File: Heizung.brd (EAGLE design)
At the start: 100 x 80 mm, 33 parts, among them IC1 MEGA8-PTQFP, Q2 2N7002, Q3 2N7002

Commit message: Floating wires are bad for you
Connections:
- removed net N$41: J_1.1, J_2.1, J_3.1, J_4.1
- net GND: now also J_1.1, J_2.1, J_3.1, J_4.1
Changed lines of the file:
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@@
 <via x="23.375" y="44.375" extent="1-16" drill="0.6" shape="square"/>
 <via x="40" y="47" extent="1-16" drill="0.6" shape="square"/>
+<contactref element="J_2" pad="1"/>
+<contactref element="J_1" pad="1"/>
+<contactref element="J_3" pad="1"/>
+<contactref element="J_4" pad="1"/>
 </signal>
 <signal name="N$141">
@@
 <wire x1="30.0823" y1="45.1461" x2="30.0823" y2="43.5055" width="0.35" layer="16"/>
 </signal>
-<signal name="N$41" class="1">
-<contactref element="J_2" pad="1"/>
-<contactref element="J_1" pad="1"/>
-<contactref element="J_3" pad="1"/>
-<contactref element="J_4" pad="1"/>
-<wire x1="40" y1="62.73" x2="40" y2="68.73" width="0" layer="19" extent="1-1"/>
-<wire x1="40" y1="56.73" x2="40" y2="62.73" width="0" layer="19" extent="1-1"/>
-<wire x1="40" y1="50.73" x2="40" y2="56.73" width="0" layer="19" extent="1-1"/>
-</signal>
 </signals>

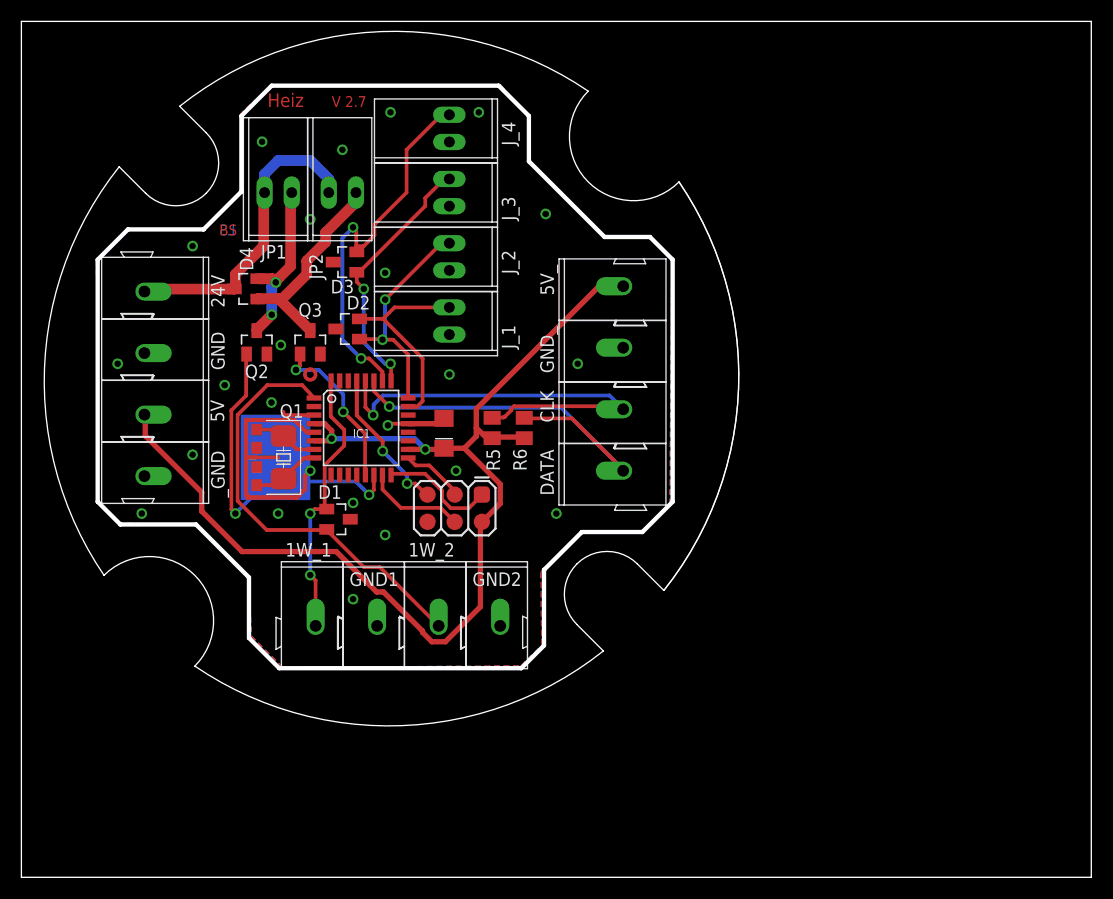
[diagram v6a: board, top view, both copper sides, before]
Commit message: 1x2 connectors wider, board outline more symmetric
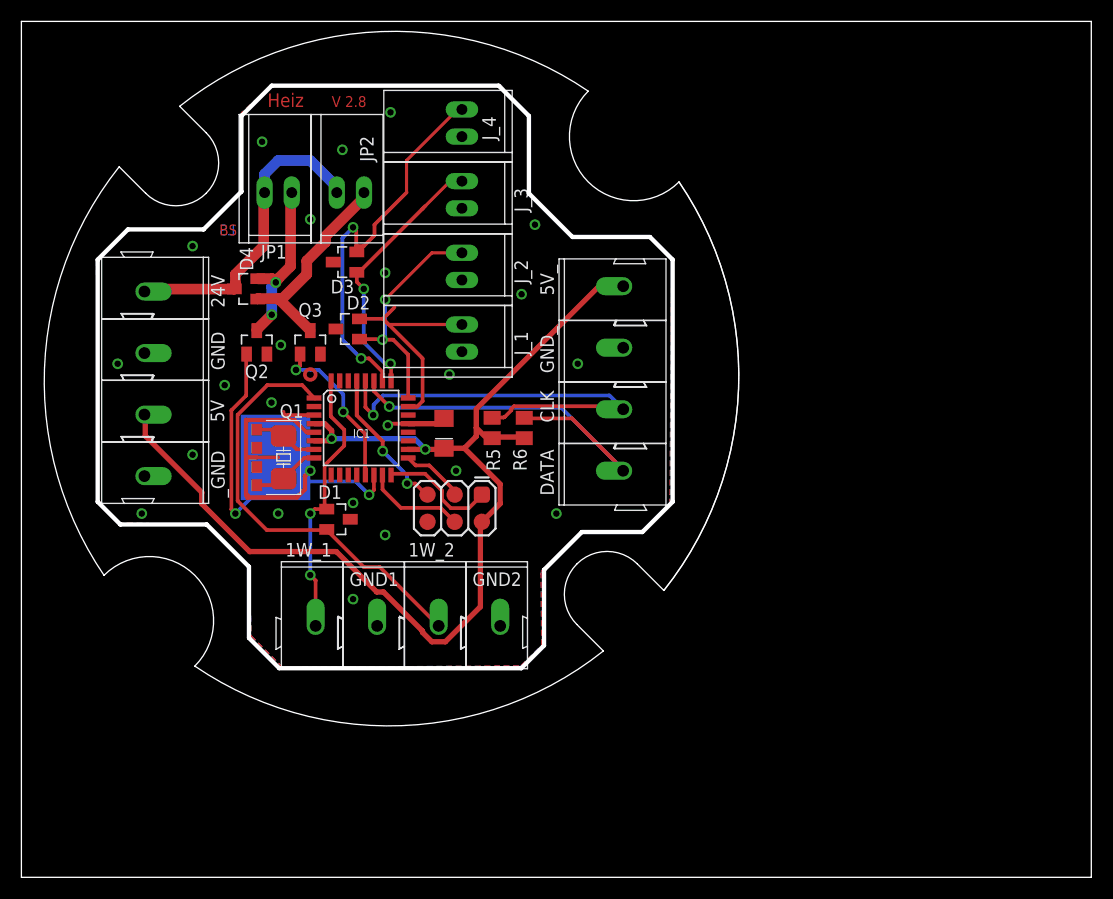
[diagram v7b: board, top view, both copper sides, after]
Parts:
- moved J_1 1.99 mm to (41.2, 50.4)
- moved J_2 1.48 mm to (41.2, 57.1)
- moved J_4 1.28 mm to (41.2, 70.5)
- moved J_3 1.19 mm to (41.2, 63.8)
- moved JP2 0.75 mm to (30.8, 64.0)
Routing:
- net B1: track 19.6 -> 21.8 mm
- net B3: track 24.5 -> 25.5 mm
- net B2: track 21.2 -> 22.0 mm
- net B4: track 35.9 -> 36.7 mm
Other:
- outline, holes or cut-outs redrawn
- board text added: "V 2.8"
- board text removed: "V 2.7"

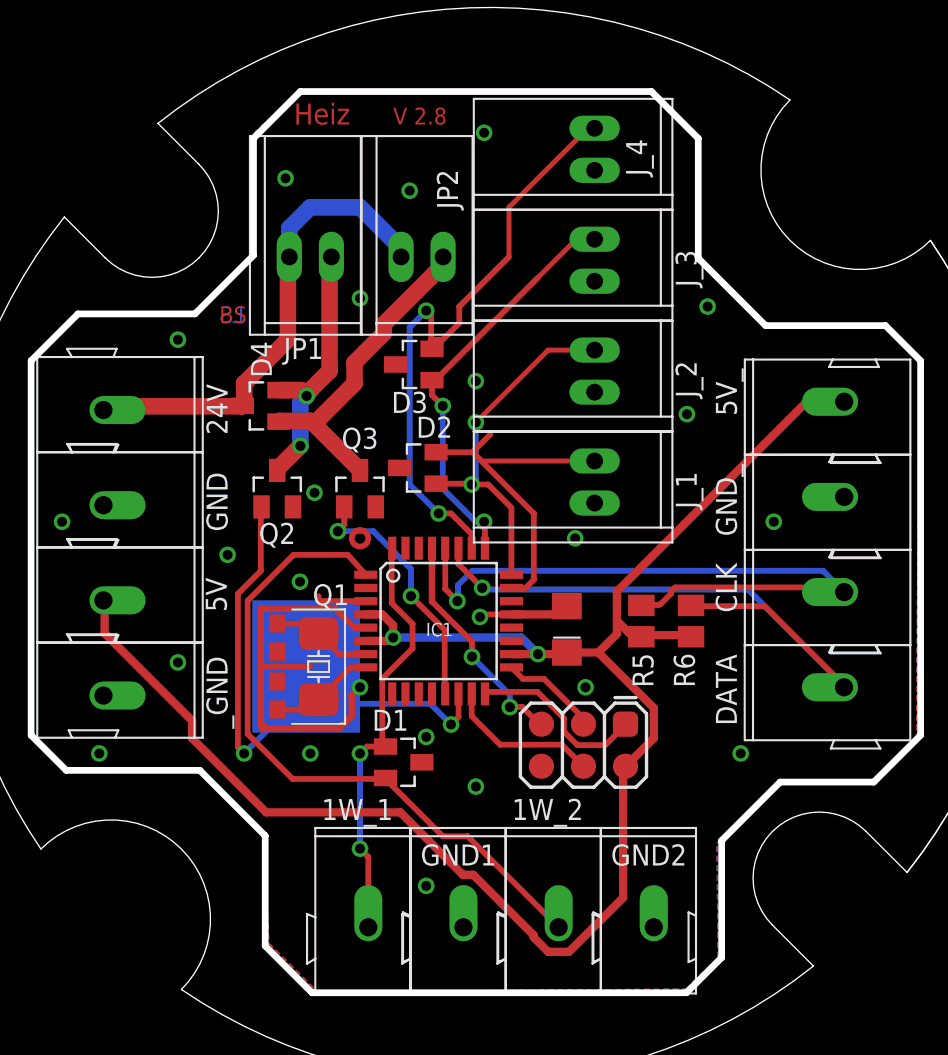
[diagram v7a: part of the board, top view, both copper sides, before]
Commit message: V2.9
add capacitor to AREF
better routing
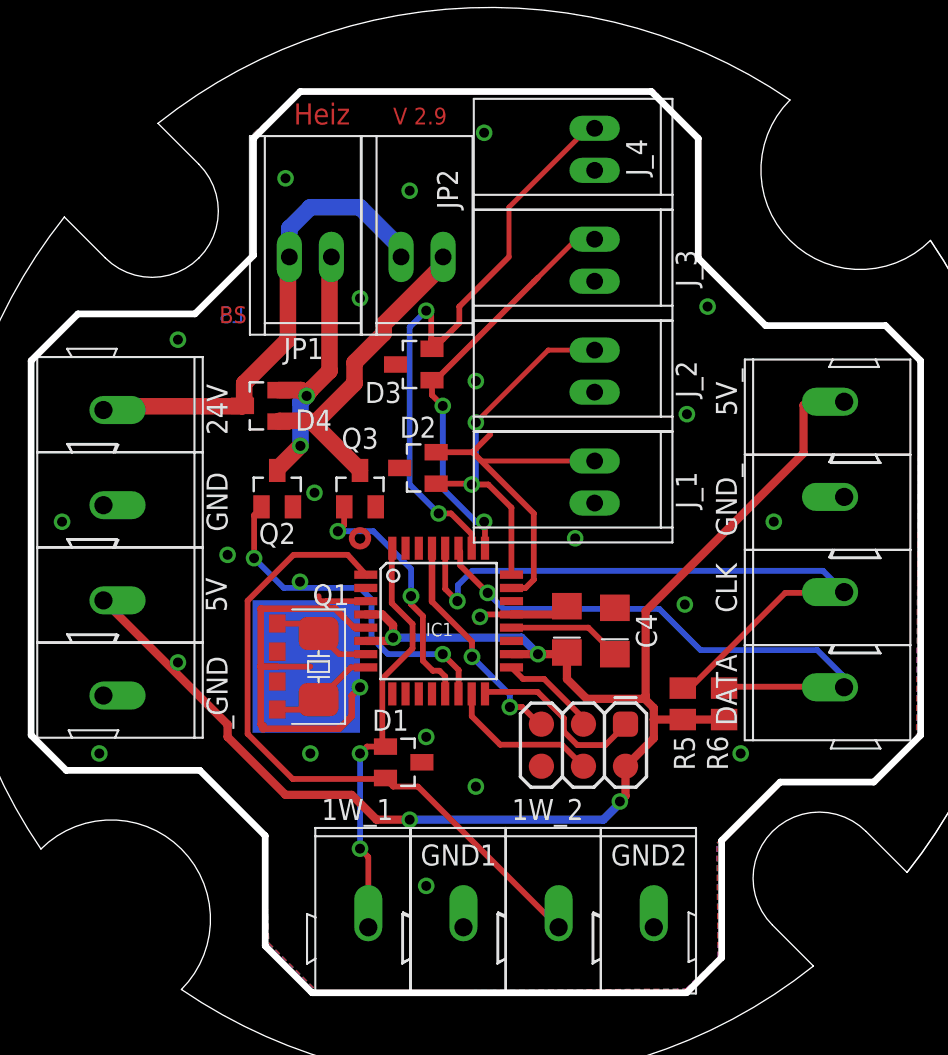
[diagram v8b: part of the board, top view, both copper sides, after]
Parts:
- added C4: 0.1µ, common:CP1206
- moved R5 5.59 mm to (46.5, 37.0)
- moved R6 5.39 mm to (49.0, 37.0)
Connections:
- new net N$41: C4.+, IC1.20
- net GND: now also C4.-
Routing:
- net N$3: track 32.0 -> 21.2 mm
- net 5V: track 107.2 -> 99.9 mm, vias 2 -> 4
- net N$41: track 0.00 -> 6.91 mm
- net N$10: track 39.0 -> 35.1 mm
- net N$18: track 41.8 -> 41.0 mm
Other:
- board text added: "V 2.9"
- board text removed: "V 2.8"
